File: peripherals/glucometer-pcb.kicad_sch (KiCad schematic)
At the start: 11 parts, among them U1 ESP32_DevKit_V1_DOIT

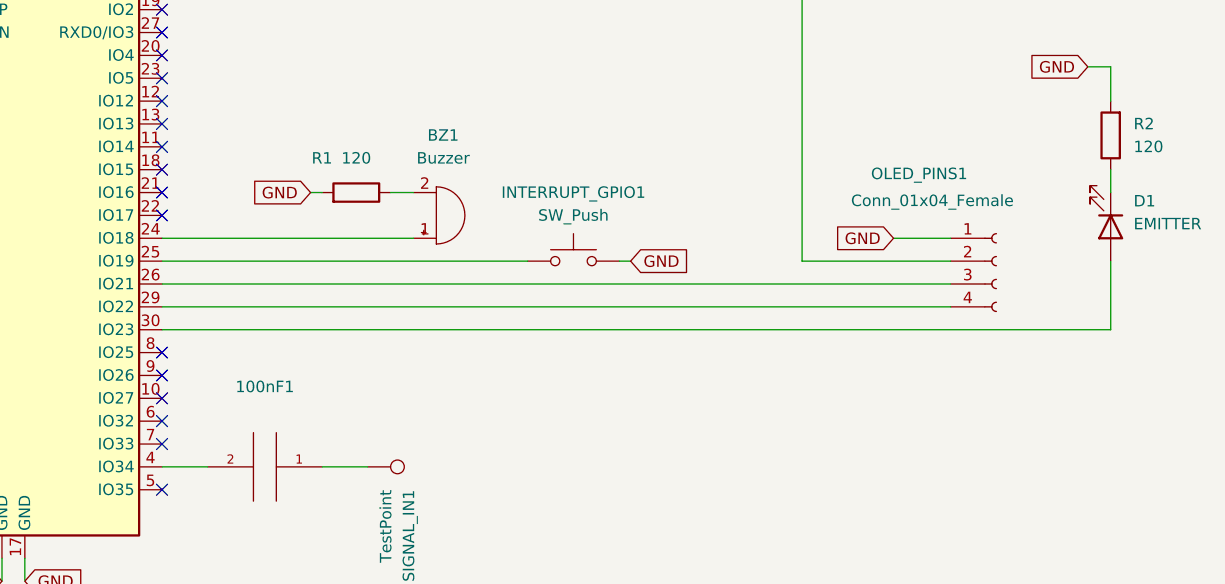
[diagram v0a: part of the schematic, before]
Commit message: peripherals pcb update
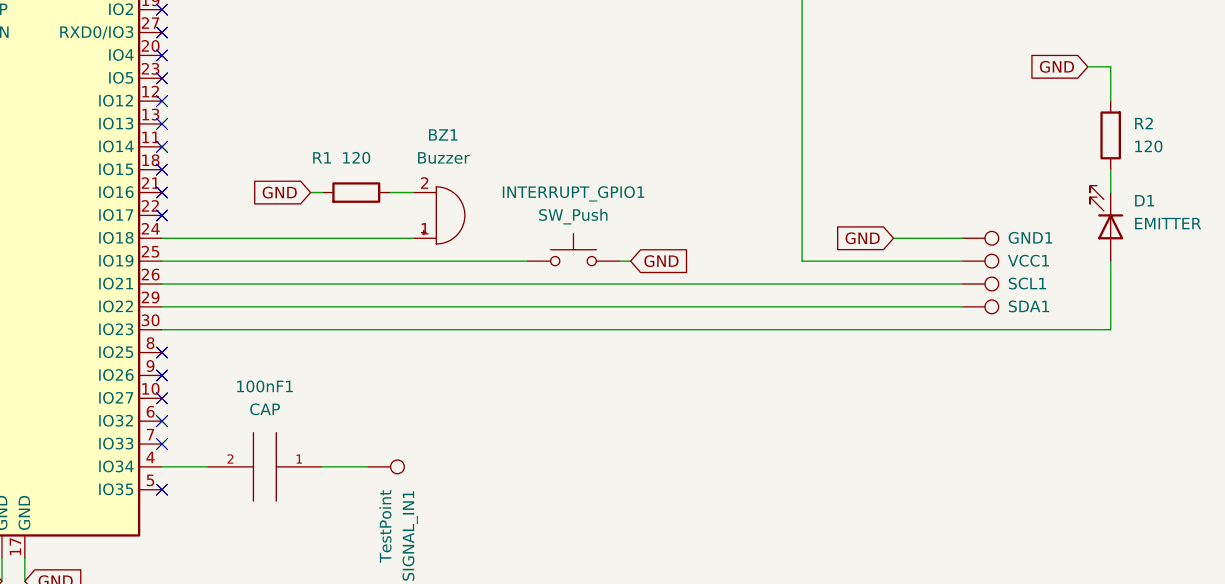
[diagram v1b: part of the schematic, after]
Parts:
- removed OLED_PINS1: Conn_01x04_Female, Connector_Wire:SolderWire-0.1sqmm_1x04_P3.6mm_D0.4mm_OD1mm, symbol Connector:Conn_01x04_Female
- added GND1, SCL1, SDA1, VCC1: (no value), symbol Connector:TestPoint
- 100nF1: value (none) -> CAP; footprint (none) -> Capacitor_THT:C_Disc_D4.3mm_W1.9mm_P5.00mm
- BZ1: footprint (none) -> Buzzer_Beeper:MagneticBuzzer_ProSignal_ABI-009-RC
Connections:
- net GND: now also GND1.1
- net at 3V3_OUT1.1, U1.16 (3V3): now also VCC1.1
- net at U1.26 (IO21): now also SCL1.1
- net at U1.29 (IO22): now also SDA1.1
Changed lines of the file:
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@@
     (stroke (width 0) (type default) (color 0 0 0 0))
   )
-  (wire (pts (xy 165.1 91.44) (xy 171.45 91.44))
+  (wire (pts (xy 165.1 91.44) (xy 172.72 91.44))
     (stroke (width 0) (type default) (color 0 0 0 0))
   )
@@
     (stroke (width 0) (type default) (color 0 0 0 0))
   )
-  (wire (pts (xy 171.45 93.98) (xy 154.94 93.98))
-    (stroke (width 0) (type default) (color 0 0 0 0))
-  )
-  (wire (pts (xy 83.82 99.06) (xy 171.45 99.06))
+  (wire (pts (xy 83.82 99.06) (xy 172.72 99.06))
     (stroke (width 0) (type default) (color 0 0 0 0))
   )
@@
     (stroke (width 0) (type default) (color 0 0 0 0))
   )
-  (wire (pts (xy 83.82 96.52) (xy 171.45 96.52))
+  (wire (pts (xy 83.82 96.52) (xy 172.72 96.52))
     (stroke (width 0) (type default) (color 0 0 0 0))
   )
   (wire (pts (xy 68.58 39.37) (xy 68.58 48.26))
+    (stroke (width 0) (type default) (color 0 0 0 0))
+  )
+  (wire (pts (xy 154.94 93.98) (xy 172.72 93.98))
     (stroke (width 0) (type default) (color 0 0 0 0))
   )
@@
     )
   )
-  (symbol (lib_id "Connector:Conn_01x04_Female") (at 176.53 93.98 0) (unit 1)
-    (in_bom yes) (on_board yes)
-    (property "Reference" "OLED_PINS1" (id 0) (at 162.5964 84.2789 0)
-      (effects (font (size 1.27 1.27)) (justify left))
-    )
-    (property "Value" "Conn_01x04_Female" (id 1) (at 160.376 87.2716 0)
-      (effects (font (size 1.27 1.27)) (justify left))
-    )
-    (property "Footprint" "Connector_Wire:SolderWire-0.1sqmm_1x04_P3.6mm_D0.4mm_OD1mm" (id 2) (at 176.53 93.98 0)
-      (effects (font (size 1.27 1.27)) hide)
-    )
-    (property "Datasheet" "~" (id 3) (at 176.53 93.98 0)
-      (effects (font (size 1.27 1.27)) hide)
-    )
-    (pin "1")
-    (pin "2")
-    (pin "3")
-    (pin "4")
-  )
   (symbol (lib_id "Device:R") (at 105.41 86.36 270) (mirror x) (unit 1)
     (in_bom yes) (on_board yes)
@@
     (in_bom yes) (on_board yes) (fields_autoplaced)
     (property "Reference" "100nF1" (id 0) (at 95.25 107.95 90))
-    (property "Value" "" (id 1) (at 95.25 110.49 90))
-    (property "Footprint" "" (id 2) (at 95.25 116.84 0)
+    (property "Value" "CAP" (id 1) (at 95.25 110.49 90))
+    (property "Footprint" "Capacitor_THT:C_Disc_D4.3mm_W1.9mm_P5.00mm" (id 2) (at 95.25 116.84 0)
       (effects (font (size 1.27 1.27)) hide)
     )
@@
     (pin "1")
     (pin "2")
+  )
+  (symbol (lib_id "Connector:TestPoint") (at 172.72 91.44 270) (mirror x) (unit 1)
+    (in_bom yes) (on_board yes)
+    (property "Reference" "GND1" (id 0) (at 177.8 91.44 90)
+      (effects (font (size 1.27 1.27)) (justify left))
+    )
+    (property "Value" "" (id 1) (at 171.45 86.36 90)
+      (effects (font (size 1.27 1.27)) (justify left))
+    )
+    (property "Footprint" "" (id 2) (at 172.72 86.36 0)
+      (effects (font (size 1.27 1.27)) hide)
+    )
+    (property "Datasheet" "~" (id 3) (at 172.72 86.36 0)
+      (effects (font (size 1.27 1.27)) hide)
+    )
+    (pin "1")
   )
   (symbol (lib_id "Device:LED") (at 189.23 90.17 270) (unit 1)
@@
     (property "Reference" "BZ1" (id 0) (at 115.062 80.01 0))
     (property "Value" "Buzzer" (id 1) (at 115.062 82.55 0))
-    (property "Footprint" "" (id 2) (at 113.665 91.44 90)
+    (property "Footprint" "Buzzer_Beeper:MagneticBuzzer_ProSignal_ABI-009-RC" (id 2) (at 113.665 91.44 90)
       (effects (font (size 1.27 1.27)) hide)
     )
@@
     )
     (property "Datasheet" "~" (id 3) (at 106.68 111.76 0)
+      (effects (font (size 1.27 1.27)) hide)
+    )
+    (pin "1")
+  )
+  (symbol (lib_id "Connector:TestPoint") (at 172.72 93.98 270) (mirror x) (unit 1)
+    (in_bom yes) (on_board yes)
+    (property "Reference" "VCC1" (id 0) (at 177.8 93.98 90)
+      (effects (font (size 1.27 1.27)) (justify left))
+    )
+    (property "Value" "" (id 1) (at 171.45 86.36 90)
+      (effects (font (size 1.27 1.27)) (justify left))
+    )
+    (property "Footprint" "" (id 2) (at 172.72 88.9 0)
+      (effects (font (size 1.27 1.27)) hide)
+    )
+    (property "Datasheet" "~" (id 3) (at 172.72 88.9 0)
       (effects (font (size 1.27 1.27)) hide)
     )
@@
     (pin "9")
   )
+  (symbol (lib_id "Connector:TestPoint") (at 172.72 99.06 270) (mirror x) (unit 1)
+    (in_bom yes) (on_board yes)
+    (property "Reference" "SDA1" (id 0) (at 177.8 99.06 90)
+      (effects (font (size 1.27 1.27)) (justify left))
+    )
+    (property "Value" "" (id 1) (at 171.45 86.36 90)
+      (effects (font (size 1.27 1.27)) (justify left))
+    )
+    (property "Footprint" "" (id 2) (at 172.72 93.98 0)
+      (effects (font (size 1.27 1.27)) hide)
+    )
+    (property "Datasheet" "~" (id 3) (at 172.72 93.98 0)
+      (effects (font (size 1.27 1.27)) hide)
+    )
+    (pin "1")
+  )
+  (symbol (lib_id "Connector:TestPoint") (at 172.72 96.52 270) (mirror x) (unit 1)
+    (in_bom yes) (on_board yes)
+    (property "Reference" "SCL1" (id 0) (at 177.8 96.52 90)
+      (effects (font (size 1.27 1.27)) (justify left))
+    )
+    (property "Value" "" (id 1) (at 171.45 86.36 90)
+      (effects (font (size 1.27 1.27)) (justify left))
+    )
+    (property "Footprint" "" (id 2) (at 172.72 91.44 0)
+      (effects (font (size 1.27 1.27)) hide)
+    )
+    (property "Datasheet" "~" (id 3) (at 172.72 91.44 0)
+      (effects (font (size 1.27 1.27)) hide)
+    )
+    (pin "1")
+  )
   (sheet_instances
     (path "/" (page "1"))
@@
       (reference "D1") (unit 1) (value "EMITTER") (footprint "LED_THT:LED_D3.0mm_Clear")
     )
+    (path "/316369ce-281e-4fab-8ad5-3b8ffc87cc69"
+      (reference "GND1") (unit 1) (value "TestPoint") (footprint "TestPoint:TestPoint_Pad_2.0x2.0mm")
+    )
     (path "/aa939002-c65a-4bc5-8b33-1d5bc4c91f9d"
       (reference "INTERRUPT_GPIO1") (unit 1) (value "SW_Push") (footprint "Connector_Wire:SolderWire-0.1sqmm_1x02_P3.6mm_D0.4mm_OD1mm")
     )
-    (path "/17943bf5-792b-4782-9dc5-99d729a45b6a"
-      (reference "OLED_PINS1") (unit 1) (value "Conn_01x04_Female") (footprint "Connector_Wire:SolderWire-0.1sqmm_1x04_P3.6mm_D0.4mm_OD1mm")
-    )
     (path "/225941a7-3d5e-4d24-af67-57772850c878"
       (reference "R1") (unit 1) (value "120") (footprint "Resistor_THT:R_Axial_DIN0204_L3.6mm_D1.6mm_P7.62mm_Horizontal")
@@
       (reference "R2") (unit 1) (value "120") (footprint "Resistor_THT:R_Axial_DIN0204_L3.6mm_D1.6mm_P7.62mm_Horizontal")
     )
+    (path "/edfe03e7-ddfb-487d-a89a-705a447b0f7c"
+      (reference "SCL1") (unit 1) (value "TestPoint") (footprint "TestPoint:TestPoint_Pad_2.0x2.0mm")
+    )
+    (path "/dcb4fd5c-8e8b-4cea-90fe-9a2746a7720a"
+      (reference "SDA1") (unit 1) (value "TestPoint") (footprint "TestPoint:TestPoint_Pad_2.0x2.0mm")
+    )
     (path "/61259d1a-256c-4970-9afa-3c8c42ac6410"
       (reference "SIGNAL_IN1") (unit 1) (value "TestPoint") (footprint "TestPoint:TestPoint_Keystone_5015_Micro-Minature")
@@
       (reference "U1") (unit 1) (value "ESP32_DevKit_V1_DOIT") (footprint "esp32_devkit_v1_doit:esp32_devkit_v1_doit")
     )
-  )
+    (path "/6590b3d2-3930-4d72-bb92-1fea5b678c21"
+      (reference "VCC1") (unit 1) (value "TestPoint") (footprint "TestPoint:TestPoint_Pad_2.0x2.0mm")
+    )
+  )
